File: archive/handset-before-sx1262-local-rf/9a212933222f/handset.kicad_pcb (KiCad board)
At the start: 4 copper layers, 66 x 142 mm, 281 parts, among them J1 2053380002, J10 LF_COIL_TUNING_REQUIRED, J16 EXPANSION_J16, J2 PACK_NTC_10K_B3435, J20 LORA_915_ANT, J21 CC1101_915_ANT, J22 GNSS_PASSIVE_ANT, J23 DM3D-SF, J24 TSAL6400_CASE_LED, J25 TSOP38438_CASE_RX, J26 FH12A-50S-0.5SH(55), J3 MEDIA_SPEAKER_DIFFERENTIAL, J4 CALL_AUDIO_FROM_MODEM_ADAPTER, J5 CALL_EARPIECE, J6 CALL_MIC, J7 PIM447_HARNESS_VERIFY, J8 MODEM_ADAPTER_3V3_LOGIC, J9 MODEM_POWER_ADAPTER_REQUIRED, Q1 AO3400A, Q3 AO3400A, Q4 AO3400A, Q5 AO3400A, Q6 AO3401A, Q7 AO3400A, Q8 AO3400A, SW1 1, SW10 10, SW11 11, SW12 12, SW13 13, SW14 14, SW15 15, SW16 16, SW17 MCU_BOOT, SW18 MCU_EN, SW19 POWER, SW2 2, SW3 3, SW4 4, SW5 5, SW6 6, SW7 7, SW8 8, SW9 9, U1 ESP32-S3-WROOM-1-N16R8, U10 TPS61023DRLR, U11 TPS62840DLCR, U12 MAX-M10S-00B-01, U13 ST25R3916B-AQET, U14 TPS2553DBVR, U15 TPD4E05U06DQAR, U16 TPD4E05U06DQAR, U17 TPD4E05U06DQAR, U18 SN74AHCT125PWR, U19 SN74LVC1G17DBVR, U2 TCA8418RTWR, U20 TPS63070RNMR, U21 TPS25200DRVR, U22 TUSB320LAIRWBR, U23 TLV70433DBVR, U24 TCA9536DGKR, U25 STM32G031G8U6, U26 TPS7A0230PDBVR, U27 TCA9800DGKR, U28 TPS7A2030PDBVR, U29 SN74LVC244APWR, U3 BQ25186DLHR, U30 SN74LVC2G125DCUR, U31 TCA9406DCUR, U32 CAT4004AHU2-GT3, U33 TCA9537DGSR, U34 SN74CB3Q3245PWR, U35 SN74HCS10PWR, U36 0900FM15K0039001E, U37 BGS12WN6E6327, U4 SX1262IMLTRT, U5 CC1101RGPR, U6 MAX98357AETE+, U7 TPS63802DLAR, U8 MAX17048G+T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

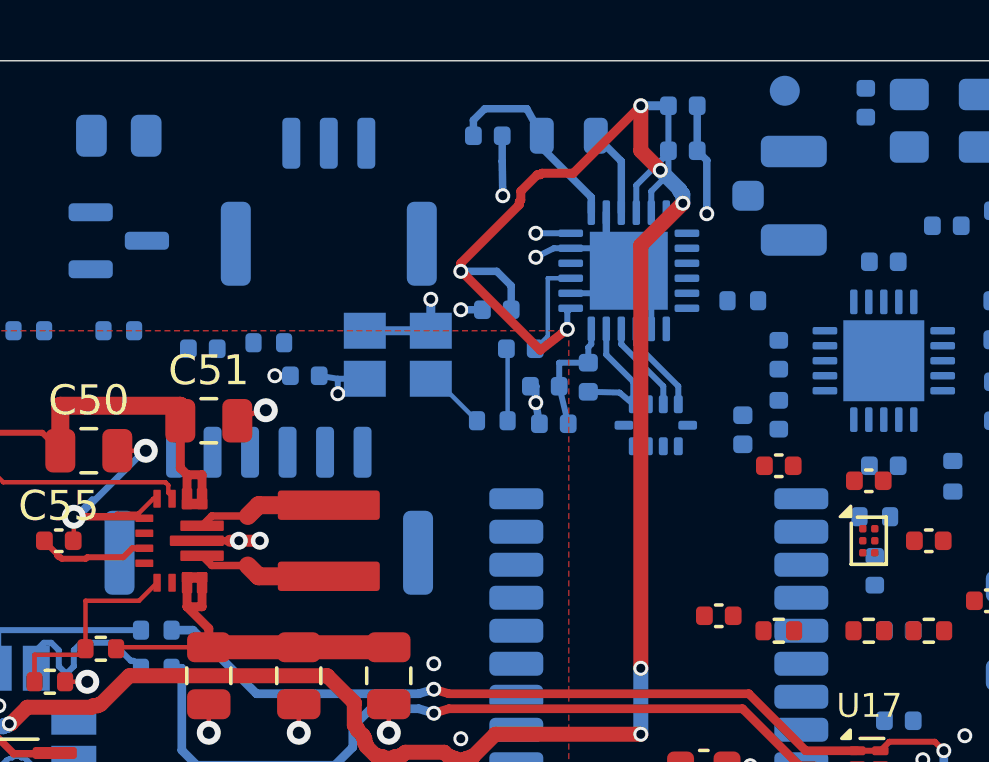
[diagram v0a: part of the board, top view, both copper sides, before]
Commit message: feat: route SX1262 local PA and RF inputs
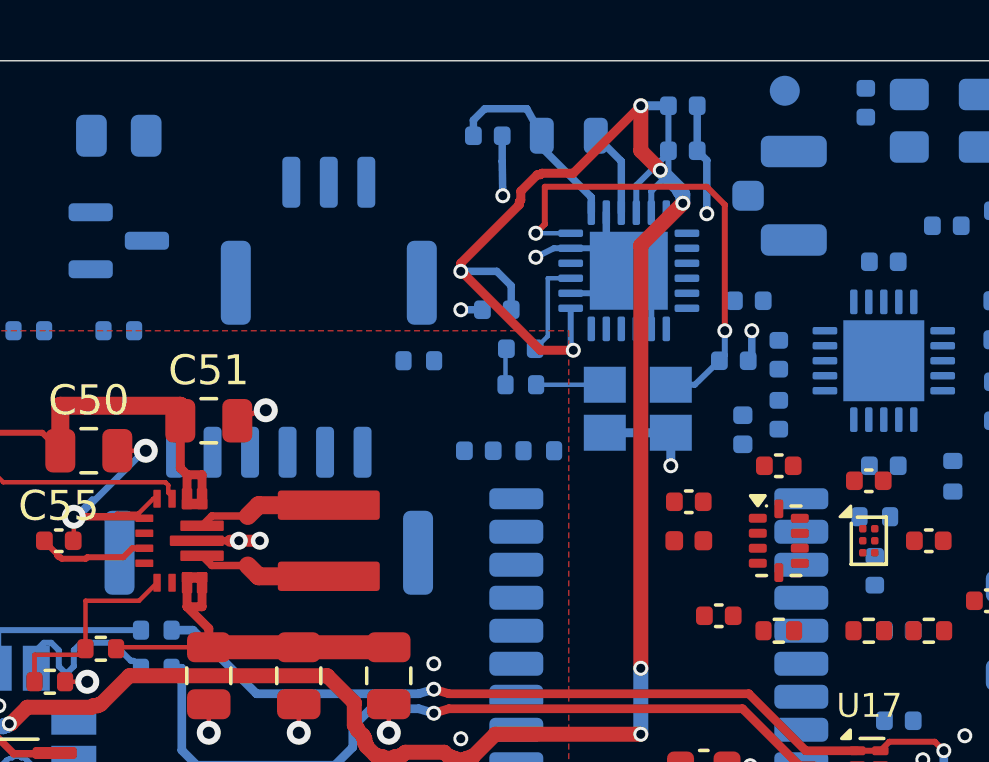
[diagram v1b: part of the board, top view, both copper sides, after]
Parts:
- C101, L13, U36: moved to F.Cu
- moved C94 14.3 mm to (116.5, 39.0), turned to 0 degrees
- moved C44 9.81 mm to (108.0, 42.0)
- moved R10 8.44 mm to (110.0, 42.0)
- moved Y3 8.20 mm to (113.3, 40.6), turned to 180 degrees
- moved C10 7.69 mm to (117.0, 37.0), turned to 0 degrees
- moved L13 6.40 mm to (115.0, 45.0), turned to 0 degrees
- moved C101 6.15 mm to (115.0, 43.7), turned to 0 degrees
- moved U36 5.62 mm to (118.0, 45.0), turned to 0 degrees
- moved R49 5.04 mm to (106.0, 39.0)
- moved R90 1.53 mm to (109.4, 39.8), turned to 180 degrees
- moved J25 1.30 mm to (103.0, 35.0)
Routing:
- net SX_RFO: track 4.53 -> 0.00 mm
- net SX_VR_PA: track 4.21 -> 0.00 mm
- net SX_RFI_P: track 3.09 -> 0.00 mm
- net SX_RFI_N: track 3.09 -> 0.00 mm
- net SX_TCXO_PWR: track 13.8 -> 16.3 mm
- net SX_TCXO_COUPLED: track 2.42 -> 1.21 mm
- net GND: track 414.3 -> 413.5 mm, vias 178 -> 177
- net +3V3: track 496.0 -> 496.6 mm
